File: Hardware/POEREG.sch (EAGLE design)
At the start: 9 parts, among them J1 SJCN

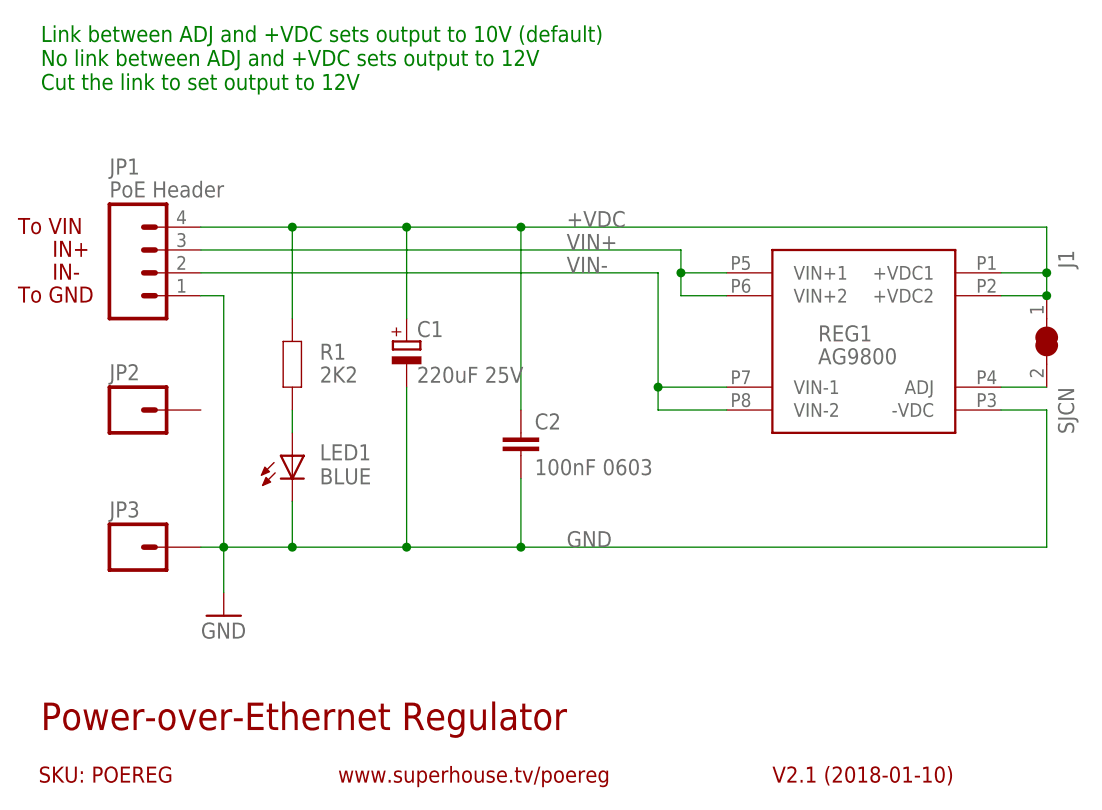
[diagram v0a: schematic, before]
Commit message: Replace Silvertel module with AG9912LP.
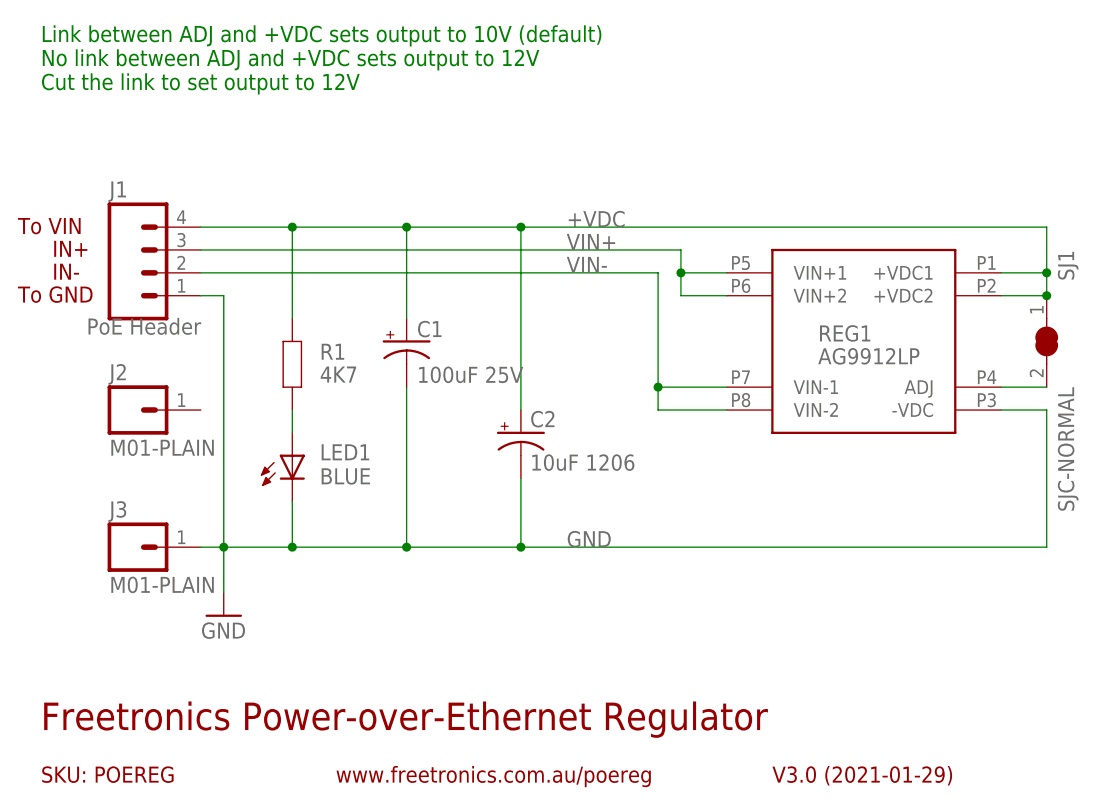
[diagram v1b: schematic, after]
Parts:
- removed JP1: PoE Header, freetronics:M04PTH
- removed JP2, JP3: M01PTH, freetronics:M01PTH
- added J2, J3: M01-PLAIN, SuperHouse-Connectors:M01-PLAIN
- added SJ1: SJC-NORMAL, SuperHouse-Jumpers:SJC-NORMAL
- C1: value 220uF 25V -> 100uF 25V; device rcl:CPOL-EUD -> SuperHouse-DiscreteSemi:CAP_POLD
- C2: value 100nF 0603 -> 10uF 1206; device freetronics-master-v1.1:CAP0603 -> SuperHouse-DiscreteSemi:CAP_POL1206
- J1: value SJCN -> PoE Header; device freetronics-jon:SJCN -> SuperHouse-Connectors:M04-PLAIN
- LED1: device freetronics:LED0603 -> SuperHouse-LEDs:LED0603
- R1: value 2K2 -> 4K7; device freetronics:RESISTOR0603 -> SuperHouse-DiscreteSemi:RESISTOR0603
- REG1: value AG9800 -> AG9912LP; device freetronics-jon:AG9800 -> SuperHouse-Regulators:AG9900-LP
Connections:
- net +VDC: now also C2.+, J1.4, SJ1.1; no longer C2.1, J1.1, JP1.4
- net GND: now also C2.-, J1.1, J3.1; no longer C2.2, JP1.1, JP3.1
- net N$1: now also SJ1.2; no longer J1.2
- net VIN+: now also J1.3; no longer JP1.3
- net VIN-: now also J1.2; no longer JP1.2
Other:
- note added: "Freetronics Power-over-Ethernet Regulator"
- note added: "V3.0 (2021-01-29)"
- note added: "www.freetronics.com.au/poereg"
- note removed: "Power-over-Ethernet Regulator"
- note removed: "V2.1 (2018-01-10)"
- note removed: "www.superhouse.tv/poereg"
